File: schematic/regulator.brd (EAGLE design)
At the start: 62 x 43 mm, 22 parts, among them J1 COMM, J2 STOP_LIGHT, Q1 NMOSFETSOT23, Q2 NMOSFETSOT23, Q3 NMOSFETSOT23, U1 MAX5035DIP8

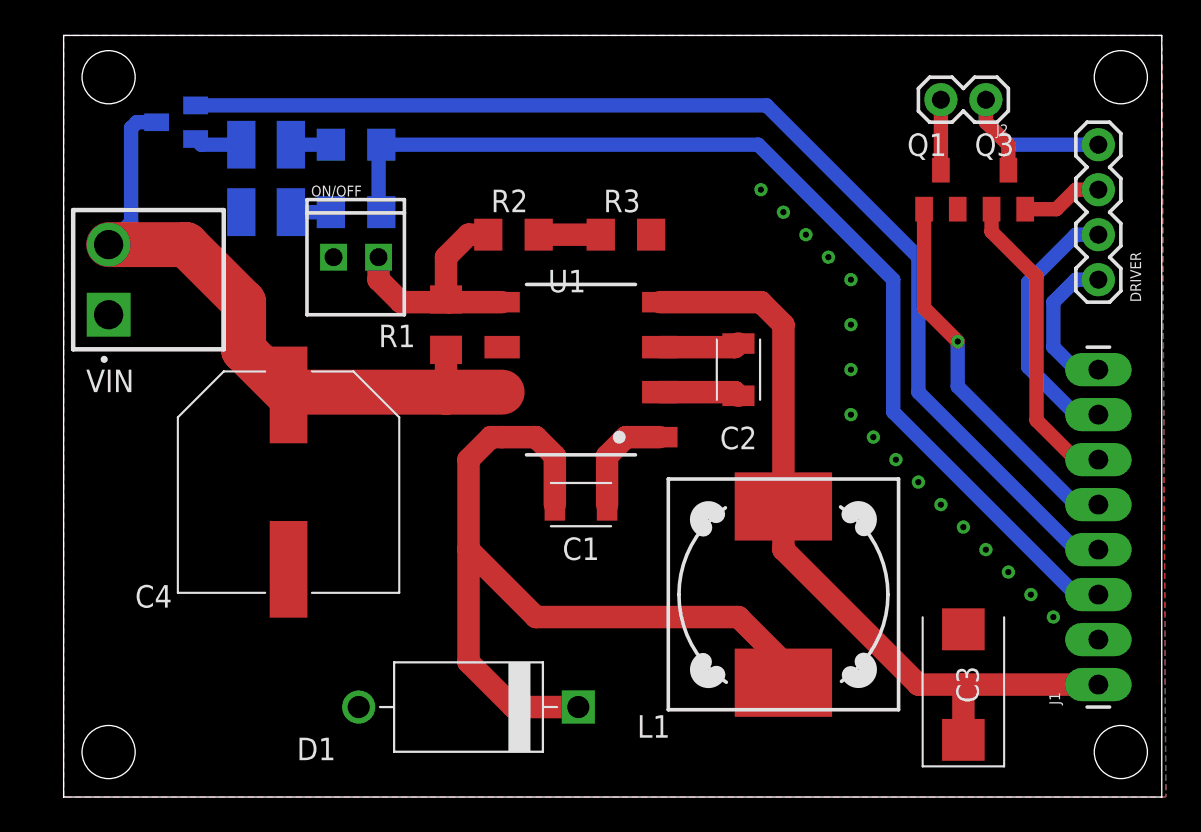
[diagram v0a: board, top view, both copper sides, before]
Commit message: Update schematics
- Add TVS diodes for ESD protection
- Add resistors on MOSFET gates
- Make voltage divider on 2 resistors(4 previously)
- Align signal names on regulator and ECU schematics
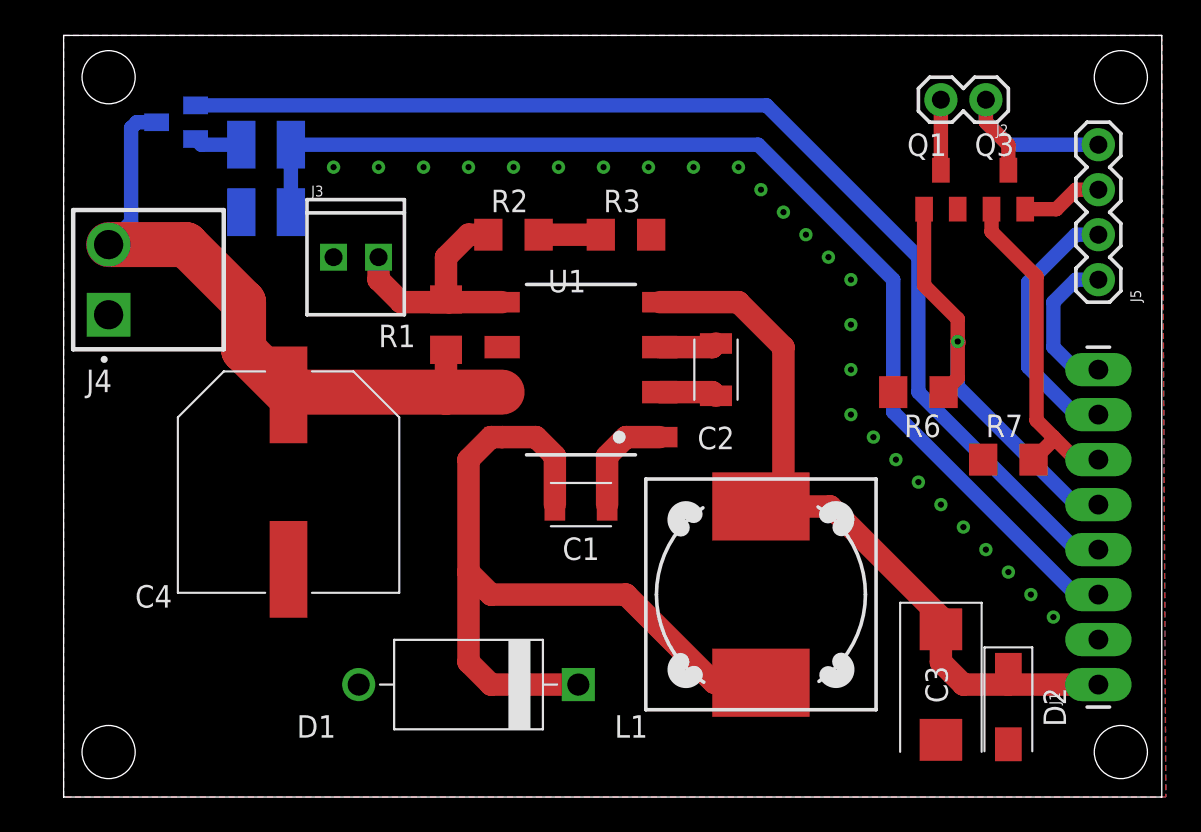
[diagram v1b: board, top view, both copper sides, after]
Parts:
- added D2: P4SMAJ12CA, eScooter:DIOM5027X220N
- J3: value (none) -> ON/OFF
- J4: value B2P-VH(LF)(SN) -> IN
- J5: value (none) -> DRIVER
- R5: value 100K -> 133K
- R6: value 22K -> 10K
- R7: value 47K -> 10K
- moved R7 40.9 mm to (53.3, 19.1), flipped to the top, turned to 0 degrees
- moved R6 33.3 mm to (48.3, 22.9), flipped to the top
- moved C2 1.27 mm to (36.8, 24.1)
- moved L1 1.27 mm to (39.4, 11.4)
- moved D1 1.27 mm to (22.9, 6.35)
- moved C3 1.27 mm to (49.5, 6.35), turned to 270 degrees
- renumbered DRIVER to J5, ON/OFF to J3, VIN to J4
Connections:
- removed net N$6: R4.1, R7.1
- removed net N$9: R5.2, R6.1
- removed net VOUT: C3.1, J1.1, L1.2, U1.4
- new net 12V: C3.1, D2.1, J1.1, L1.2, U1.4
- net BAT: now also R4.1, R5.2; no longer R6.2, R7.2
- net GND: now also D2.2, R6.2, R7.1
- net STLEDCTL: now also R6.1
- net STOUT: now also R7.2
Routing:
- net VOUT: track 44.3 -> 0.00 mm
- net 12V: track 0.00 -> 43.1 mm
- net BAT: track 59.3 -> 64.3 mm
- net STLEDCTL: track 21.5 -> 24.9 mm
- net N$2: track 48.8 -> 45.8 mm
- net N$9: track 2.26 -> 0.00 mm
- net N$6: track 2.26 -> 0.00 mm
- net STOUT: track 17.4 -> 19.1 mm
- net N$4: track 4.53 -> 3.26 mm
- net GND: track 4.53 -> 3.26 mm, vias 17 -> 27

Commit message: Update schematics for regulator
- Add elements nominals and correct values
- Fix library inconsistence
- Few cosmetical changes in schematics
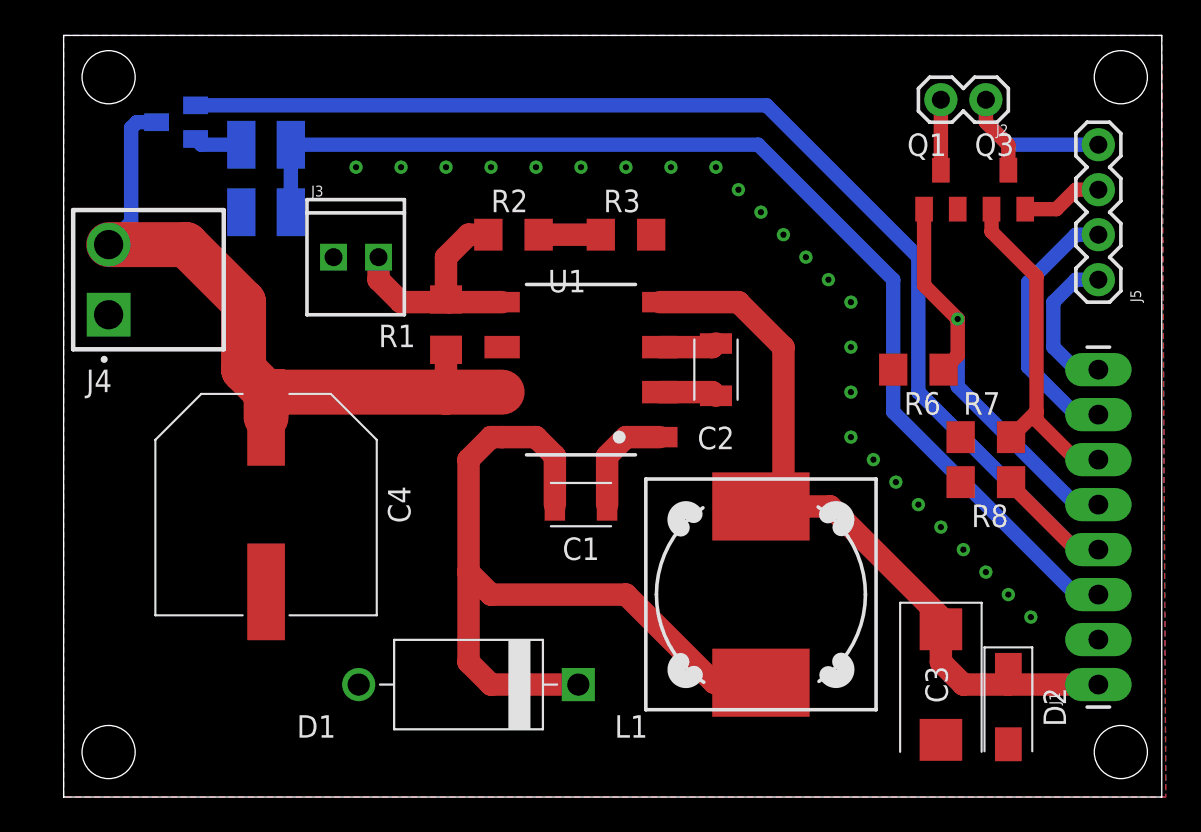
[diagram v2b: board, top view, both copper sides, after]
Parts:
- added R8: 10K, eagle-ltspice:R1206
- C1, C2: value (none) -> 0.1uF
- C3: value (none) -> 15uF
- C4: value CPANASONIC_H13 -> 68uF; device regulator:CAPAE1230X1250N -> eScooter:CAPAE1230X1250N
- D1: value MBR360G -> SB5100
- moved R7 1.80 mm to (52.1, 20.3)
- moved C4 1.80 mm to (11.4, 16.5)
- moved R6 1.27 mm to (48.3, 24.1)
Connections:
- net GND: now also R8.2
- net PWM: now also R8.1
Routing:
- net PWM: track 65.8 -> 72.4 mm
- net VIN: track 38.5 -> 40.4 mm
- net GND: vias 27 -> 26

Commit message: Fix minor issues in PCB
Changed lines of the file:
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@@
 </element>
 <element name="J1" library="SparkFun-Connectors" library_urn="urn:adsk.eagle:library:513" package="1X08_LONGPADS" package3d_urn="urn:adsk.eagle:package:38142/1" value="COMM" x="58.42" y="6.35" smashed="yes" rot="R90">
-<attribute name="NAME" x="56.261" y="5.207" size="0.6096" layer="25" font="vector" ratio="20" rot="R90"/>
+<attribute name="NAME" x="56.261" y="7.747" size="0.6096" layer="25" font="vector" ratio="20" rot="R90"/>
 <attribute name="VALUE" x="61.214" y="5.334" size="0.6096" layer="27" font="vector" ratio="20" rot="R90"/>
 </element>
 <element name="J2" library="SparkFun-Connectors" library_urn="urn:adsk.eagle:library:513" package="1X02" package3d_urn="urn:adsk.eagle:package:38039/1" value="STOP_LIGHT" x="52.07" y="39.37" smashed="yes" rot="R180">
-<attribute name="NAME" x="53.34" y="37.973" size="0.6096" layer="25" font="vector" ratio="20" rot="R180"/>
+<attribute name="NAME" x="54.61" y="39.243" size="0.6096" layer="25" font="vector" ratio="20" rot="R180"/>
 <attribute name="VALUE" x="53.34" y="41.402" size="0.6096" layer="27" font="vector" ratio="20" rot="R180"/>
 </element>
@@
 <attribute name="MANUFACTURER" value="" x="6.35" y="38.1" size="1.778" layer="28" rot="MR270" display="off"/>
 <attribute name="MPN" value="" x="6.35" y="38.1" size="1.778" layer="28" rot="MR270" display="off"/>
-<attribute name="NAME" x="4.445" y="40.005" size="1.27" layer="26" rot="MR270"/>
+<attribute name="NAME" x="4.445" y="37.465" size="1.27" layer="26" rot="MR270"/>
 <attribute name="OPERATING_TEMP" value="" x="6.35" y="38.1" size="1.778" layer="28" rot="MR270" display="off"/>
 <attribute name="PART_STATUS" value="" x="6.35" y="38.1" size="1.778" layer="28" rot="MR270" display="off"/>

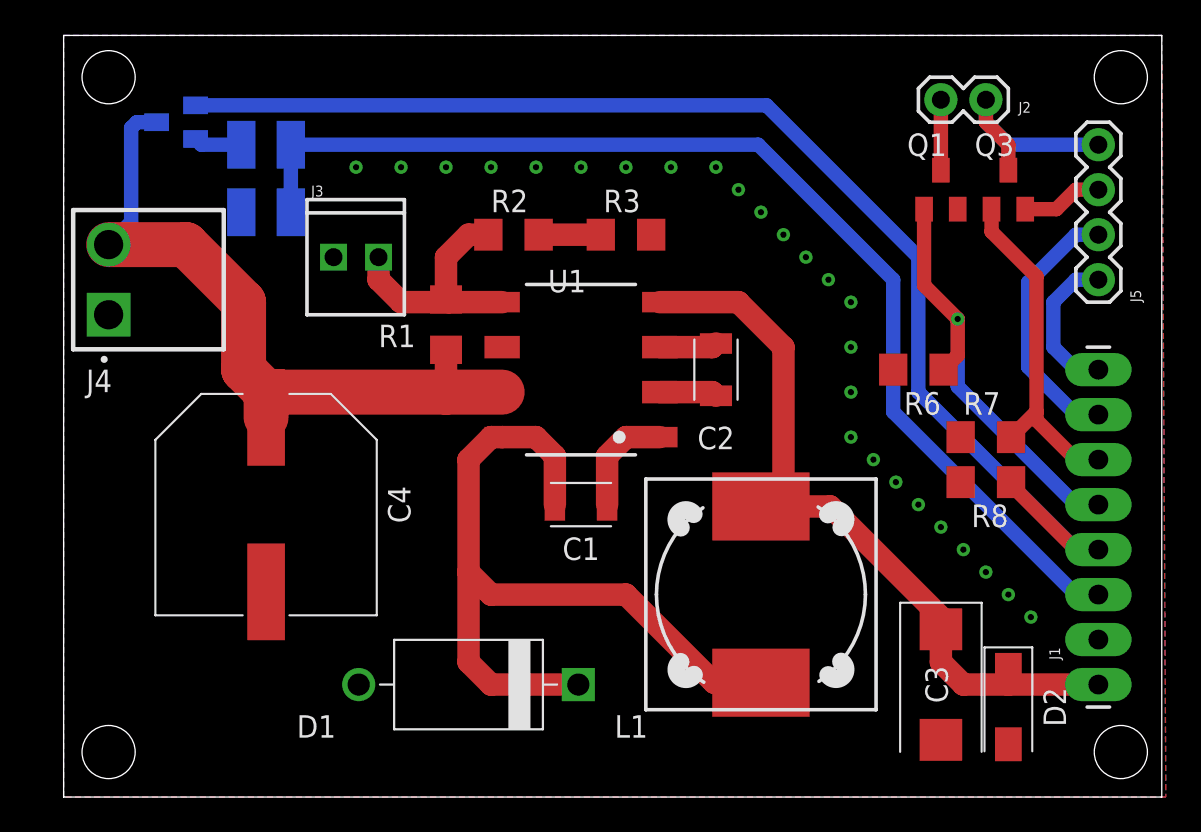
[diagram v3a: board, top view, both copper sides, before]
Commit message: Move regulator elements closer to MAX chip
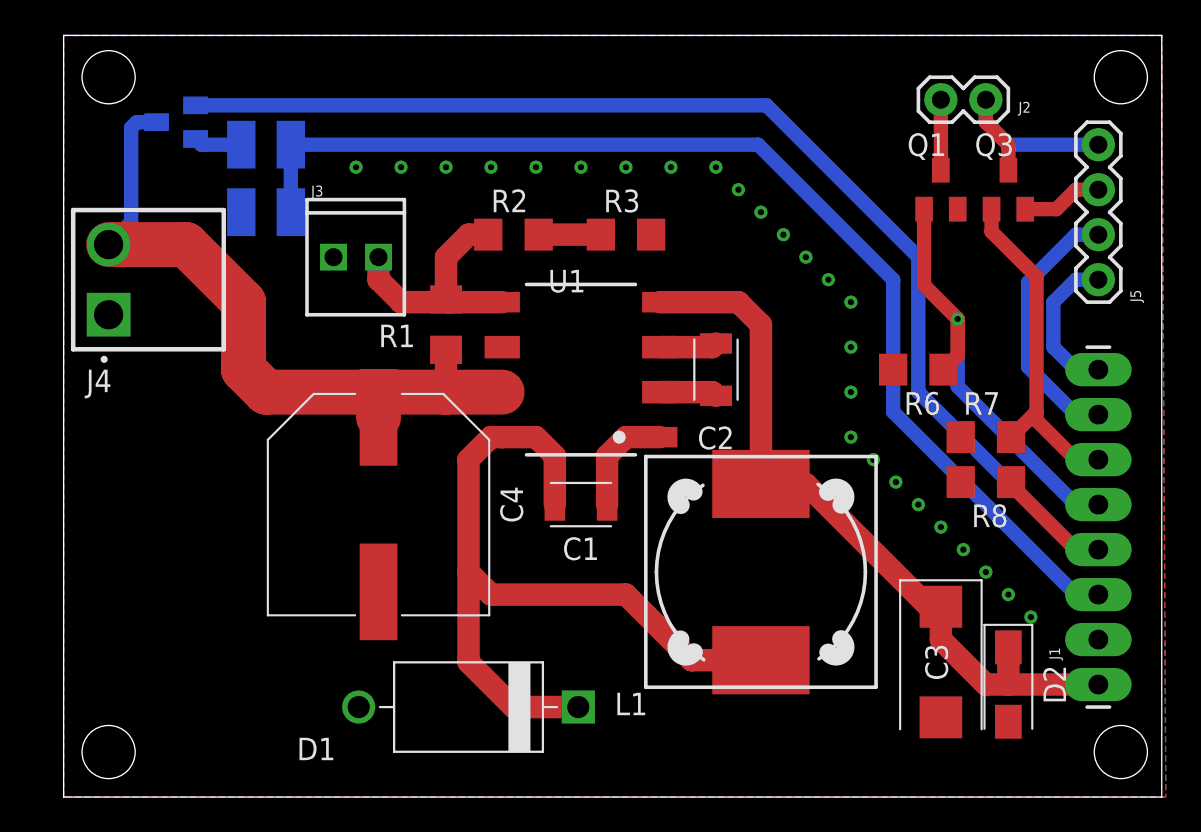
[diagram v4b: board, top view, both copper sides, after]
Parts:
- moved C4 6.35 mm to (17.8, 16.5)
- moved C3 1.27 mm to (49.5, 7.62)
- moved D1 1.27 mm to (22.9, 5.08)
- moved D2 1.27 mm to (53.3, 6.35)
- moved L1 1.27 mm to (39.4, 12.7)
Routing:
- net 12V: track 43.1 -> 42.2 mm
